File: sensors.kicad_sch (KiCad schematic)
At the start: 6 parts, among them J2 Conn_Coaxial, U14 ISM6HG256X, U3 MS5607-02BA, U5 MAX-M10S

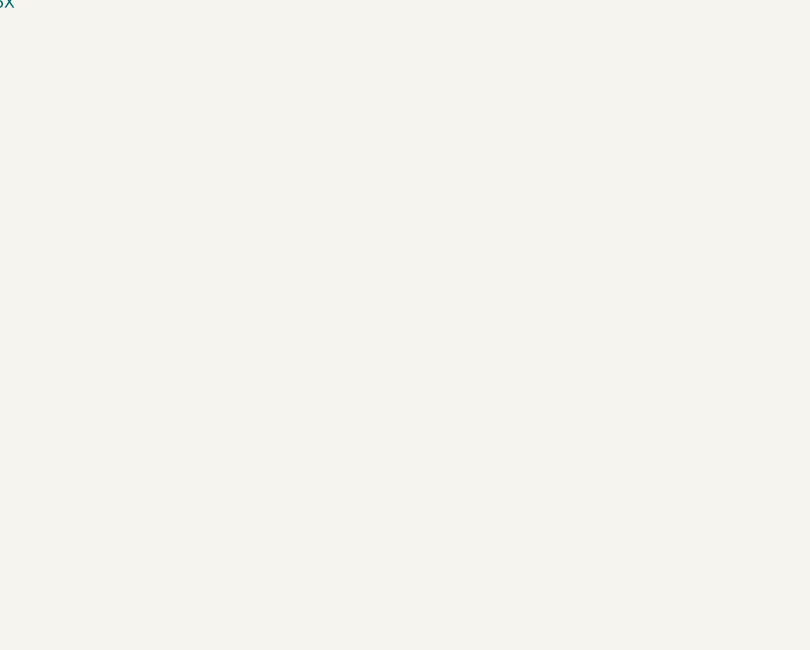
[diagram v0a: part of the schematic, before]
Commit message: update schematics and add 3d models
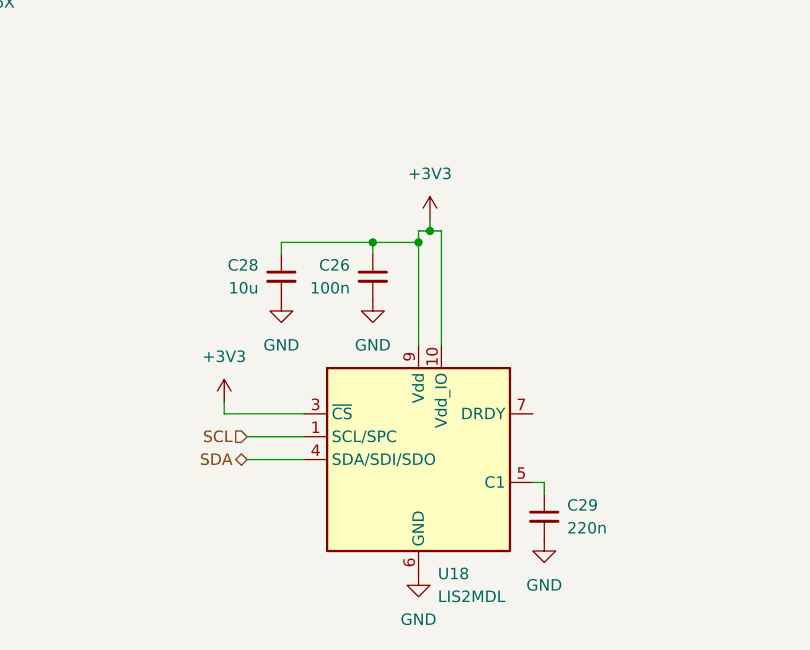
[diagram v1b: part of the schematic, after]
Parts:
- added C26: 100n, Capacitor_SMD:C_0402_1005Metric, symbol Device:C_Small
- added C28: 10u, Capacitor_SMD:C_0402_1005Metric, symbol Device:C_Small
- added C29: 220n, Capacitor_SMD:C_0402_1005Metric, symbol Device:C_Small
- added U18: LIS2MDL, Package_LGA:LGA-12_2x2mm_P0.5mm, symbol Sensor_Magnetic:LIS2MDL
- C4, C5: LCSC (none) -> C1525
- J2: footprint Connector_Coaxial:U.FL_Molex_MCRF_73412-0110_Vertical -> Connector_Coaxial:U.FL_Hirose_U.FL-R-SMT-1_Vertical; LCSC (none) -> C88374
- U3: LCSC (none) -> C97627
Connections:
- net +3V3: now also C26.1, C28.1, U18.10 (Vdd_IO), U18.3 (~{CS}), U18.9 (Vdd)
- net GND: now also C26.2, C28.2, C29.2, U18.6 (GND), U18.8 (GND)
- net SCL: now also U18.1 (SCL/SPC)
- net SDA: now also U18.4 (SDA/SDI/SDO)
- new net: C29.1, U18.5 (C1)

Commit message: change out LEDs, add silk, start getting ready for fab
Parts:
- added D10: LED, LED_SMD:LED_0805_2012Metric, symbol Device:LED
- added R11: 10, Resistor_SMD:R_0402_1005Metric, symbol Device:R_Small
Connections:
- net GND: now also D10.1 (K)
- net at U5.4 (TIMEPULSE): now also R11.1
- net EXTINT: now reaches U5.5 (EXTINT)
- new net: D10.2 (A), R11.2
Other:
- moved on the sheet: J2

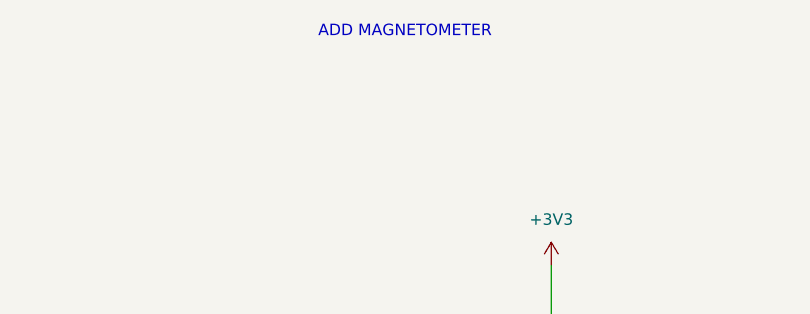
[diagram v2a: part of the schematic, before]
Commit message: capacitor spam, needs current limiting
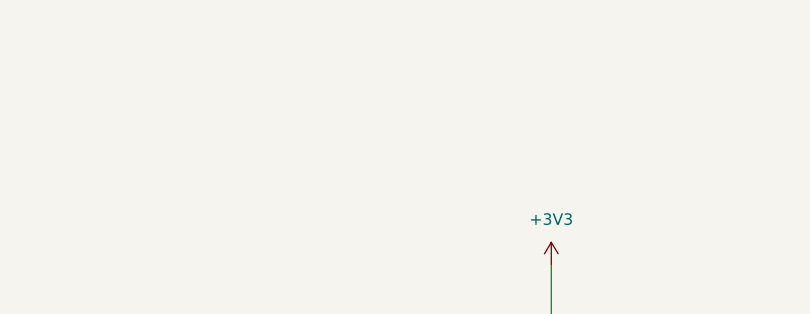
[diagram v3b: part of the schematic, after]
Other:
- note removed: "ADD MAGNETOMETER"
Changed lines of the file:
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@@
 	(generator_version "9.0")
 	(paper "A4")
-	(text "ADD MAGNETOMETER"
-		(exclude_from_sim no)
-		(at 132.334 56.642 0)
-		(effects
-			(font
-				(size 1.27 1.27)
-			)
-		)
-	)
 	(junction
 		(at 121.92 148.59)

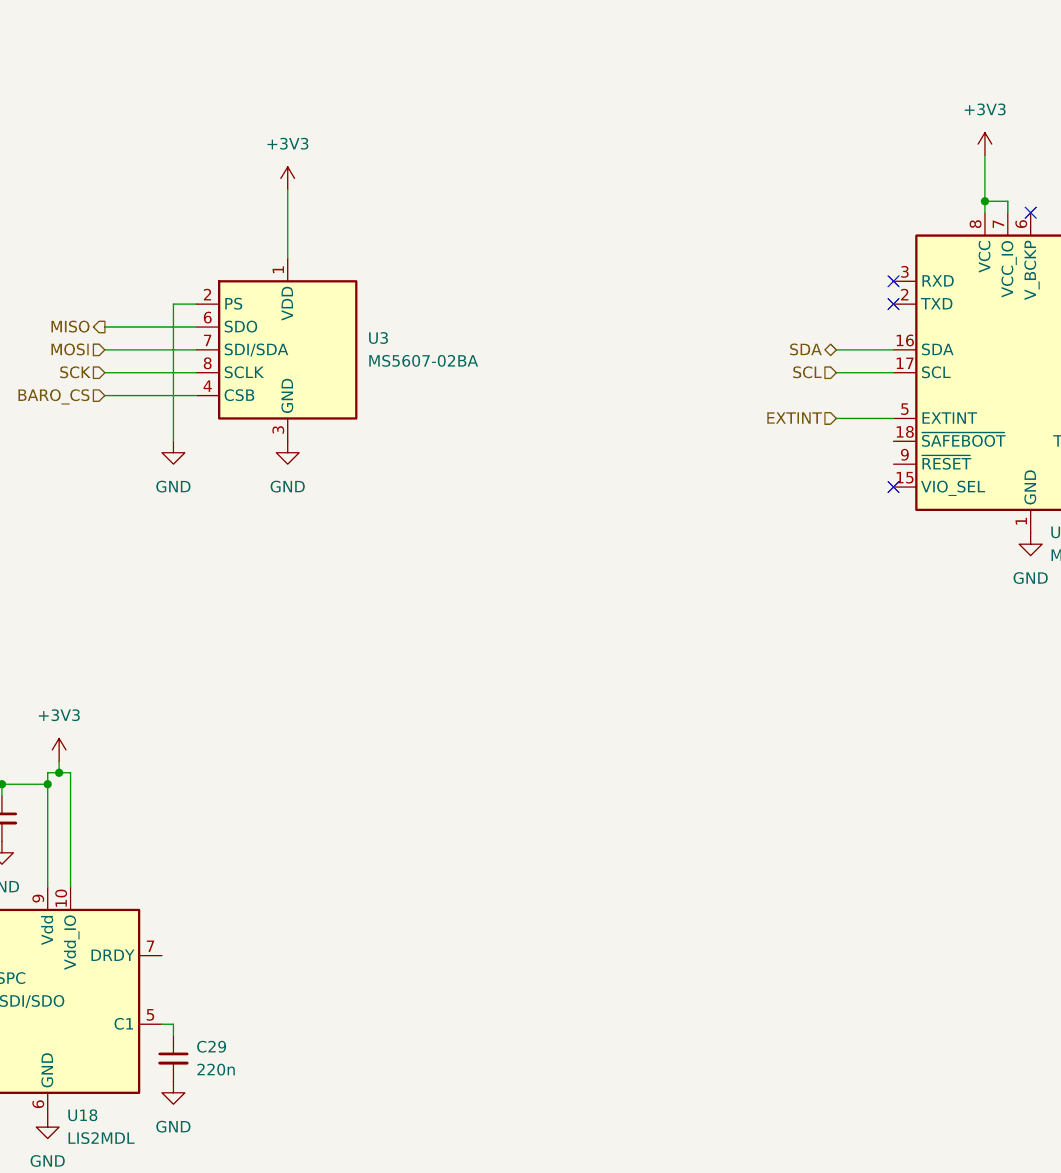
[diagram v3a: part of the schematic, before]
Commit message: finished power, checked most sensor schematics
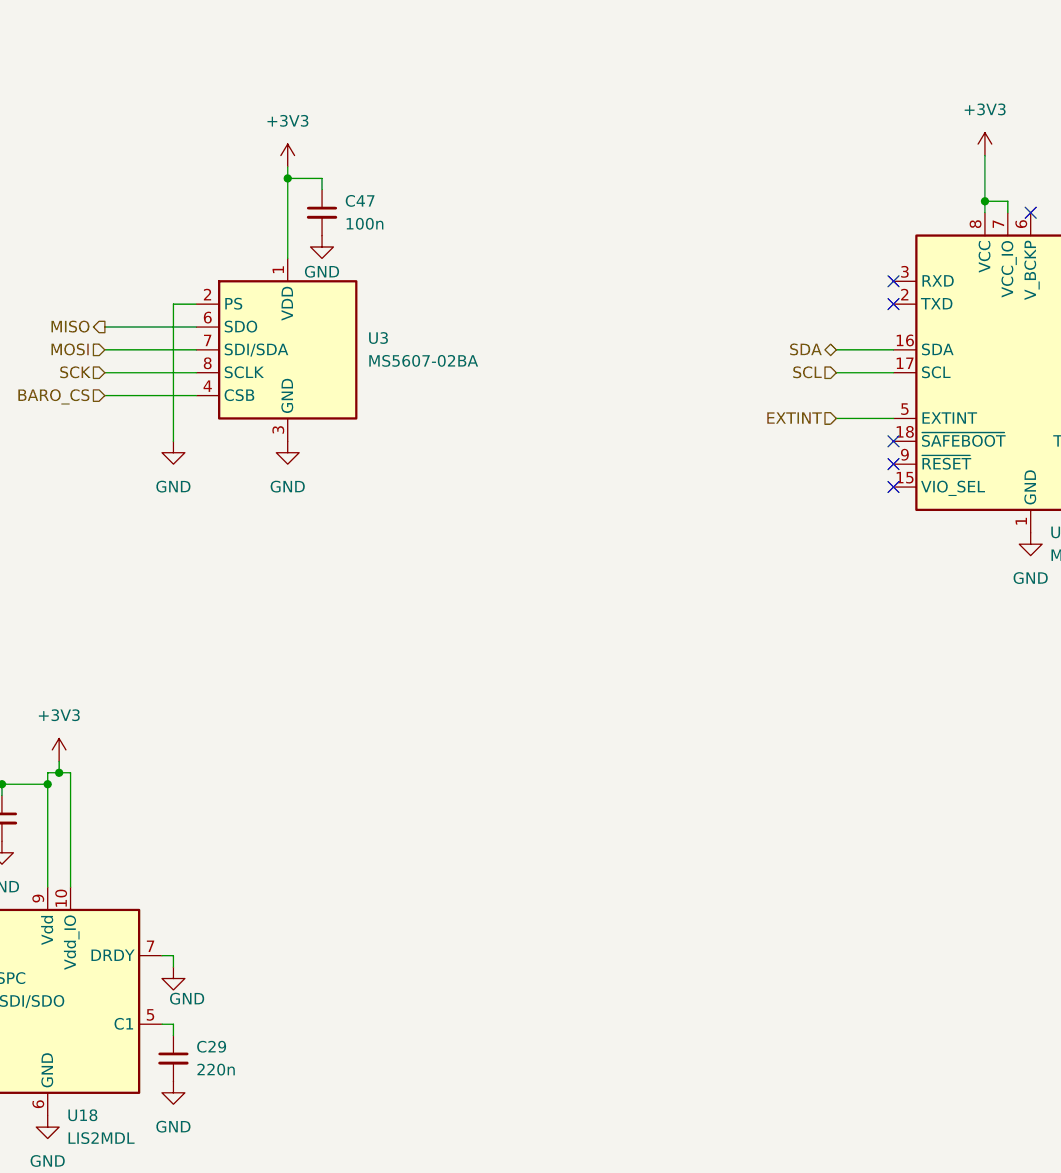
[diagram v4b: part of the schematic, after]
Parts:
- added C47: 100n, Capacitor_SMD:C_0402_1005Metric, symbol Device:C_Small
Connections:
- net +3V3: now also C47.1
- net GND: now also U18.7 (DRDY), C47.2
- no-connect marks 8 -> 10

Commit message: bigger pours for FETs, various cleanup, switching to different level shifter
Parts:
- R11: value 10 -> 120
- U14: digikey (none) -> 497-ISM6HG256XTRCT-ND
- U18: digikey (none) -> 497-17588-1-ND
- U5: digikey (none) -> 672-MAX-M10S-00BCT-ND
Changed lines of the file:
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@@
+			)
+		)
+		(property "digikey" ""
+			(at 116.84 152.4 0)
+			(effects
+				(font
+					(size 1.27 1.27)
+				)
+				(hide yes)
 			)
 		)
@@
 			)
 		)
+		(property "digikey" ""
+			(at 152.4 85.09 0)
+			(effects
+				(font
+					(size 1.27 1.27)
+				)
+				(hide yes)
+			)
+		)
 		(pin "2"
 		)
@@
 			)
 		)
+		(property "digikey" ""
+			(at 106.68 152.4 0)
+			(effects
+				(font
+					(size 1.27 1.27)
+				)
+				(hide yes)
+			)
+		)
 		(pin "1"
 		)
@@
 			)
 		)
+		(property "digikey" ""
+			(at 256.54 97.79 0)
+			(effects
+				(font
+					(size 1.27 1.27)
+				)
+				(hide yes)
+			)
+		)
 		(pin "2"
 		)
@@
 			)
 		)
+		(property "digikey" ""
+			(at 148.59 100.33 0)
+			(effects
+				(font
+					(size 1.27 1.27)
+				)
+				(hide yes)
+			)
+		)
 		(pin "5"
 		)
@@
 		)
 		(property "LCSC" ""
+			(at 231.14 102.87 0)
+			(effects
+				(font
+					(size 1.27 1.27)
+				)
+				(hide yes)
+			)
+		)
+		(property "digikey" "672-MAX-M10S-00BCT-ND"
 			(at 231.14 102.87 0)
 			(effects
@@
 			)
 		)
+		(property "digikey" "497-17588-1-ND"
+			(at 121.92 172.72 0)
+			(effects
+				(font
+					(size 1.27 1.27)
+				)
+				(hide yes)
+			)
+		)
 		(pin "10"
 		)
@@
 			)
 		)
+		(property "digikey" ""
+			(at 275.59 110.49 0)
+			(effects
+				(font
+					(size 1.27 1.27)
+				)
+				(hide yes)
+			)
+		)
 		(pin "2"
 		)
@@
 			)
 		)
+		(property "digikey" ""
+			(at 74.93 74.93 0)
+			(effects
+				(font
+					(size 1.27 1.27)
+				)
+				(hide yes)
+			)
+		)
 		(pin "2"
 		)
@@
 			)
 		)
+		(property "digikey" ""
+			(at 66.04 74.93 0)
+			(effects
+				(font
+					(size 1.27 1.27)
+				)
+				(hide yes)
+			)
+		)
 		(pin "2"
 		)
@@
 			)
 		)
+		(property "digikey" "497-ISM6HG256XTRCT-ND"
+			(at 63.5 102.87 0)
+			(effects
+				(font
+					(size 1.27 1.27)
+				)
+				(hide yes)
+			)
+		)
 		(pin "11"
 		)
@@
 		)
 		(property "LCSC" "C16772"
+			(at 135.89 179.07 0)
+			(effects
+				(font
+					(size 1.27 1.27)
+				)
+				(hide yes)
+			)
+		)
+		(property "digikey" ""
 			(at 135.89 179.07 0)
 			(effects
@@
 			)
 		)
-		(property "Value" "10"
+		(property "Value" "120"
 			(at 265.43 107.95 90)
 			(effects
@@
 			(at 265.43 110.49 90)
 			(effects
+				(font
+					(size 1.27 1.27)
+				)
+				(hide yes)
+			)
+		)
+		(property "digikey" ""
+			(at 265.43 110.49 90)
+			(effects
